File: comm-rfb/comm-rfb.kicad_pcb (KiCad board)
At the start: 4 copper layers, 90.2 x 95.9 mm, 5 parts, among them J1 PC104_Connector

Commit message: comm-rfb: reduce number of sheets in schematic
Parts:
- added C1: 12n, Capacitor_SMD:C_0402_1005Metric, F.Cu at (140.7, 115.6)
- added C10: 10p, Capacitor_SMD:C_0603_1608Metric, F.Cu at (168.4, 105.4)
- added C11: 0.1uF, Capacitor_SMD:C_0603_1608Metric, F.Cu at (192.3, 97.3)
- added C12: 10u, Capacitor_SMD:C_0603_1608Metric, F.Cu at (163.1, 112.4)
- added C13: 100n, Capacitor_SMD:C_0603_1608Metric, F.Cu at (172.4, 105.4)
- added C14: 100n, Capacitor_SMD:C_0603_1608Metric, F.Cu at (164.4, 105.4)
- added C15: 10n, Capacitor_SMD:C_0603_1608Metric, F.Cu at (167.2, 107.9)
- added C16: 1u, Capacitor_SMD:C_0603_1608Metric, F.Cu at (159.1, 112.4)
- added C17: 1u, Capacitor_SMD:C_0603_1608Metric, F.Cu at (171.2, 107.9)
- added C18: 100u, Capacitor_SMD:C_0603_1608Metric, F.Cu at (167.2, 112.9)
- added C19: 100n, Capacitor_SMD:C_0603_1608Metric, F.Cu at (177.1, 90.2)
- added C2: 20p, Capacitor_SMD:C_0402_1005Metric, F.Cu at (143.6, 111.6)
- added C20: 22u, Capacitor_SMD:C_0805_2012Metric, F.Cu at (164.8, 89.2)
- added C21: 22u, Capacitor_SMD:C_0805_2012Metric, F.Cu at (174.7, 87.5)
- added C3: 1000p, Capacitor_SMD:C_0402_1005Metric, F.Cu at (140.7, 113.6)
- added C4: 1000p, Capacitor_SMD:C_0402_1005Metric, F.Cu at (152.0, 105.1)
- added C5: 1000p, Capacitor_SMD:C_0402_1005Metric, F.Cu at (146.5, 109.6)
- added C6: 10p, Capacitor_SMD:C_0402_1005Metric, F.Cu at (143.6, 113.6)
- added C7: 10p, Capacitor_SMD:C_0402_1005Metric, F.Cu at (149.1, 107.1)
- added C8: 1p8, Capacitor_SMD:C_0402_1005Metric, F.Cu at (140.7, 111.6)
- added C9: 10p, Capacitor_SMD:C_0603_1608Metric, F.Cu at (167.2, 110.4)
- added D1: LED, LED_SMD:LED_0603_1608Metric, F.Cu at (183.0, 80.7)
- added D3: RED, Diode_SMD:D_0603_1608Metric, F.Cu at (188.4, 97.3)
- added FB1: 100R @ 100 MHz, Inductor_SMD:L_0603_1608Metric, F.Cu at (178.9, 87.2)
- added FB2: 100R @ 100MHz, Inductor_SMD:L_0603_1608Metric, F.Cu at (159.1, 109.9)
- added FB4: 100R @ 100 MHz, Daughterboard_footprints:BEADC1608X75N, F.Cu at (180.7, 101.9)
- added J10: Conn_02x04_Counter_Clockwise, Connector_PinSocket_2.54mm:PinSocket_2x04_P2.54mm_Vertical, F.Cu at (183.1, 121.7)
- added J11: Conn_02x06_Odd_Even, Connector_PinSocket_2.54mm:PinSocket_2x06_P2.54mm_Horizontal, F.Cu at (160.0, 121.7)
- added J12: Conn_02x05_Counter_Clockwise, Connector_PinSocket_2.54mm:PinSocket_2x05_P2.54mm_Horizontal, F.Cu at (175.9, 121.6)
- added J2: TFM-110-02-SM-D-A-K-TR, qset-footprints:SAMTEC_TFM-110-02-SM-D-A-K-TR, F.Cu at (130.5, 83.4)
- added J3: TFM-110-02-SM-D-A-K-TR, qset-footprints:SAMTEC_TFM-110-02-SM-D-A-K-TR, F.Cu at (149.0, 91.3)
- added J4: TFM-110-02-SM-D-A-K-TR, qset-footprints:SAMTEC_TFM-110-02-SM-D-A-K-TR, F.Cu at (130.5, 91.3)
- added J5: TFM-110-02-SM-D-A-K-TR, qset-footprints:SAMTEC_TFM-110-02-SM-D-A-K-TR, F.Cu at (149.0, 83.4)
- added J6: Conn_Coaxial, Connector_Coaxial:SMA_Amphenol_132134-10_Vertical, F.Cu at (125.5, 117.9)
- added J7: Conn_Coaxial, Connector_Coaxial:SMA_Amphenol_132134-10_Vertical, F.Cu at (134.7, 117.9)
- added J8: Conn_Coaxial, Connector_Coaxial:SMA_Amphenol_132134-10_Vertical, F.Cu at (134.7, 108.7)
- added J9: Conn_Coaxial, Connector_Coaxial:SMA_Amphenol_132134-10_Vertical, F.Cu at (125.5, 108.7)
- added L1: 150n, Inductor_SMD:L_0402_1005Metric, F.Cu at (149.1, 105.2)
- added L2: 22n, Inductor_SMD:L_0402_1005Metric, F.Cu at (143.6, 109.7)
- added MAX4372F1: MAX4372FESA+, STM32_Breakout:SOIC127P600X175-8N, F.Cu at (176.7, 82.7)
- added R1: 9.1k, Resistor_SMD:R_0603_1608Metric, F.Cu at (145.7, 105.4)
- added R10: 10k, Resistor_SMD:R_0603_1608Metric, F.Cu at (163.1, 109.9)
- added R2: 330, Resistor_SMD:R_0402_1005Metric, F.Cu at (140.7, 109.7)
- added R3: 15, Resistor_SMD:R_0402_1005Metric, F.Cu at (145.1, 107.7)
- added R4: 1k5, Resistor_SMD:R_0603_1608Metric, F.Cu at (183.0, 83.2)
- added R5: 100m, Resistor_SMD:R_0603_1608Metric, F.Cu at (173.1, 90.2)
- added R9: 2.2k, Resistor_SMD:R_0603_1608Metric, F.Cu at (184.7, 101.9)
- added TP1: TestPoint, TestPoint:TestPoint_Pad_D2.0mm, F.Cu at (169.1, 89.7)
- added U1: STM32F030CCT6, qset-footprints:QFP50P900X900X160-48N, F.Cu at (192.0, 73.9)
- added U2: SKY67150-396LF, qset-footprints:SON50P200X200X80-9N, F.Cu at (141.5, 105.9)
- added U3: AMS1117-3.3, Package_TO_SOT_SMD:SOT-223-3_TabPin2, F.Cu at (167.5, 83.5)
- added U4: MCP9808T-E/MC, qset-footprints:MCP9808T-E&slash_MC, F.Cu at (193.8, 111.8)
- added Y1: 16 MHz, Crystal:Crystal_SMD_3225-4Pin_3.2x2.5mm, F.Cu at (159.8, 106.4)
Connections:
- J1 pad 1: unconnected-(J1-Pad1) -> COMM-TXD
- J1 pad 2: unconnected-(J1-Pad2) -> COMM-RXD
- J1 pad 3: unconnected-(J1-Pad3) -> COMM-CTS
- J1 pad 32: unconnected-(J1-Pad32) -> 5V0-CHG
- J1 pad 4: unconnected-(J1-Pad4) -> COMM-RTS
- J1 pad 61: unconnected-(J1-Pad61) -> GND
- J1 pad 66: unconnected-(J1-Pad66) -> GND
- J1 pad 67: unconnected-(J1-Pad67) -> SW6-5V
- J1 pad 69: unconnected-(J1-Pad69) -> GND
- J1 pad 72: unconnected-(J1-Pad72) -> GND
- J1 pad 73: unconnected-(J1-Pad73) -> GND
- J1 pad 74: unconnected-(J1-Pad74) -> GND
- J1 pad 81: unconnected-(J1-Pad81) -> GND
- J1 pad 82: unconnected-(J1-Pad82) -> GND
- J1 pad 84: unconnected-(J1-Pad84) -> GND

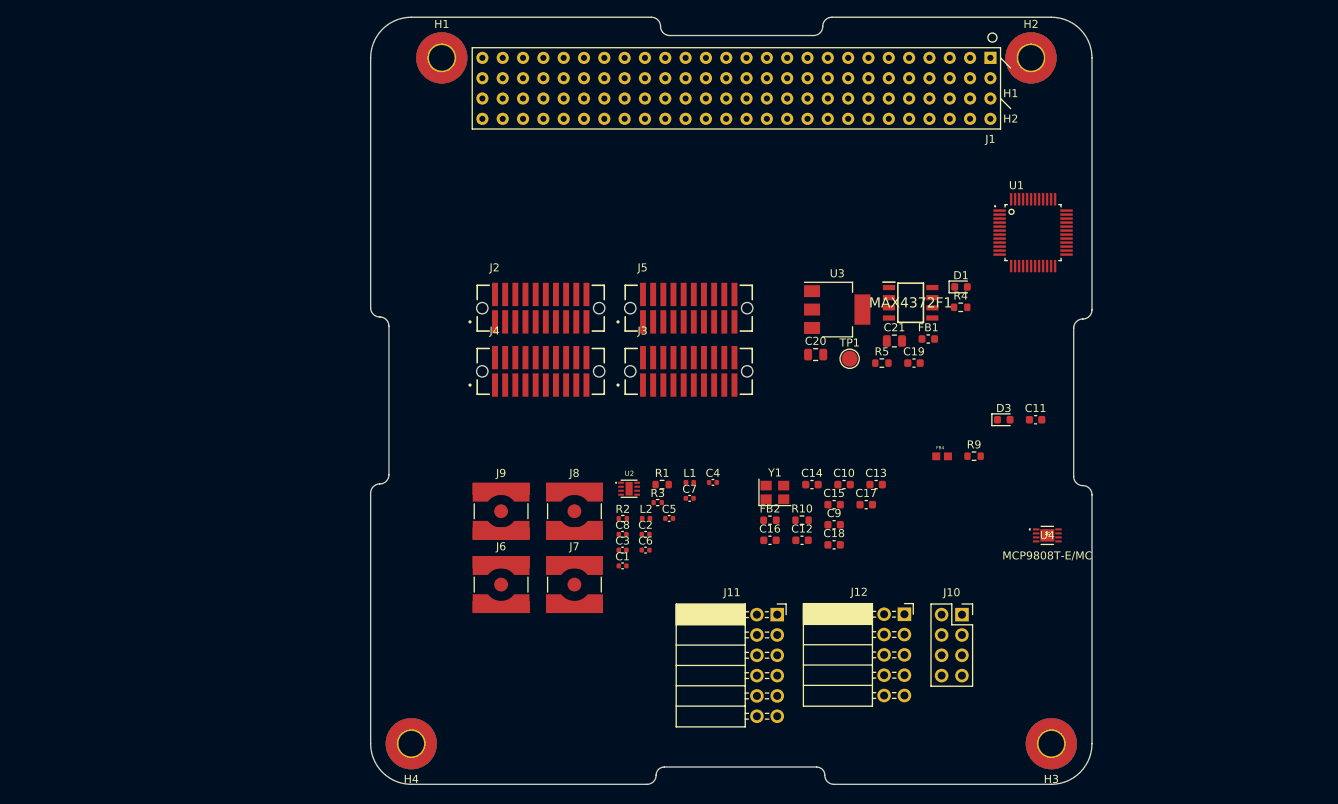
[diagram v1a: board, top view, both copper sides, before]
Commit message: possible layout -no connections
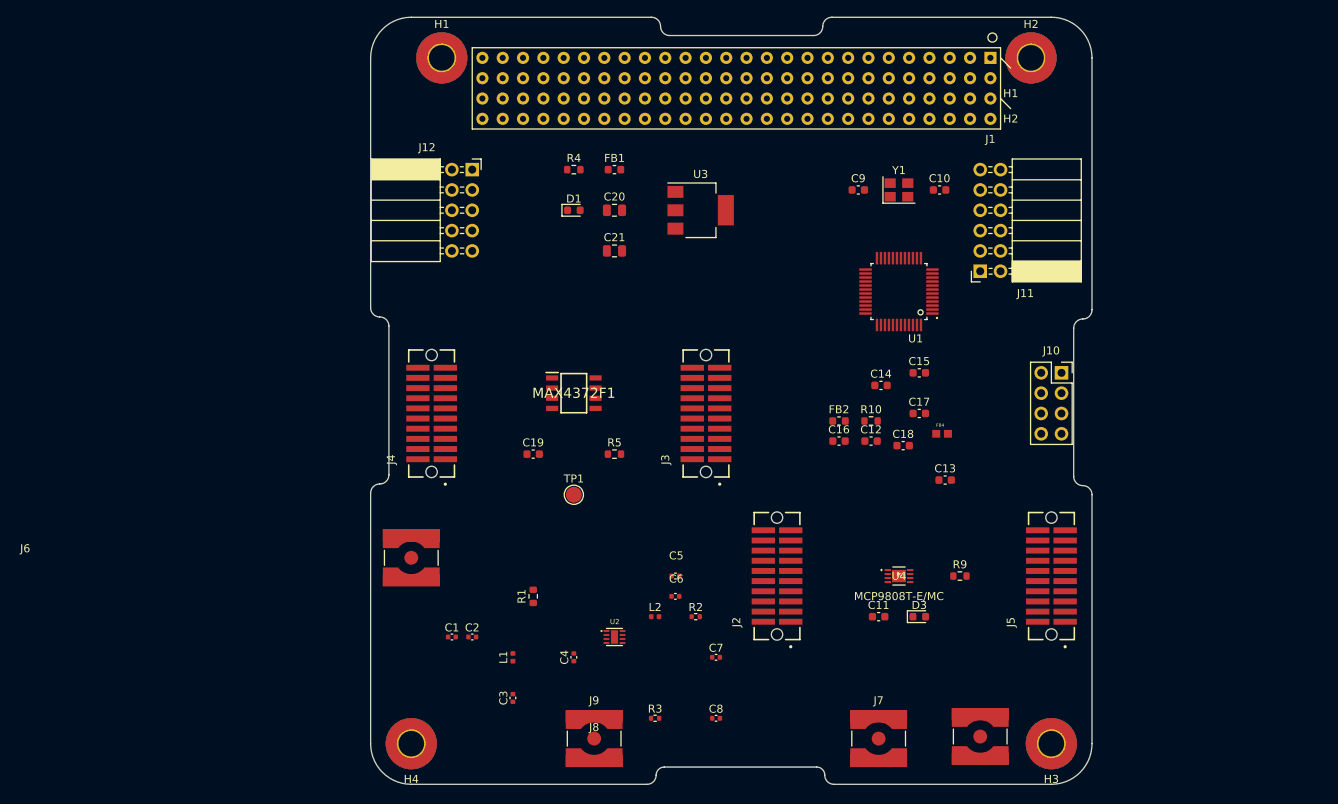
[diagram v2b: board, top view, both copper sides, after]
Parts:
- moved J12 77.5 mm to (121.9, 66.0)
- moved J8 58.0 mm to (185.4, 136.9)
- moved J5 56.4 mm to (194.3, 116.8), turned to 90 degrees
- moved R4 51.3 mm to (134.6, 66.0)
- moved J11 49.9 mm to (185.4, 78.7), turned to 180 degrees
- moved D1 49.3 mm to (134.6, 71.1)
- moved C19 48.9 mm to (129.5, 101.6)
- moved J2 44.7 mm to (160.0, 116.8), turned to 90 degrees
- moved FB1 44.6 mm to (139.7, 66.0)
- moved MAX4372F1 43.6 mm to (134.6, 94.0)
- moved J7 42.6 mm to (172.7, 137.2)
- moved C9 42.0 mm to (170.2, 68.6)
- moved Y1 40.9 mm to (175.3, 68.6)
- moved C10 38.7 mm to (180.3, 68.6)
- moved TP1 38.4 mm to (134.6, 106.7)
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
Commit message: initial routing done ~ fix bug still
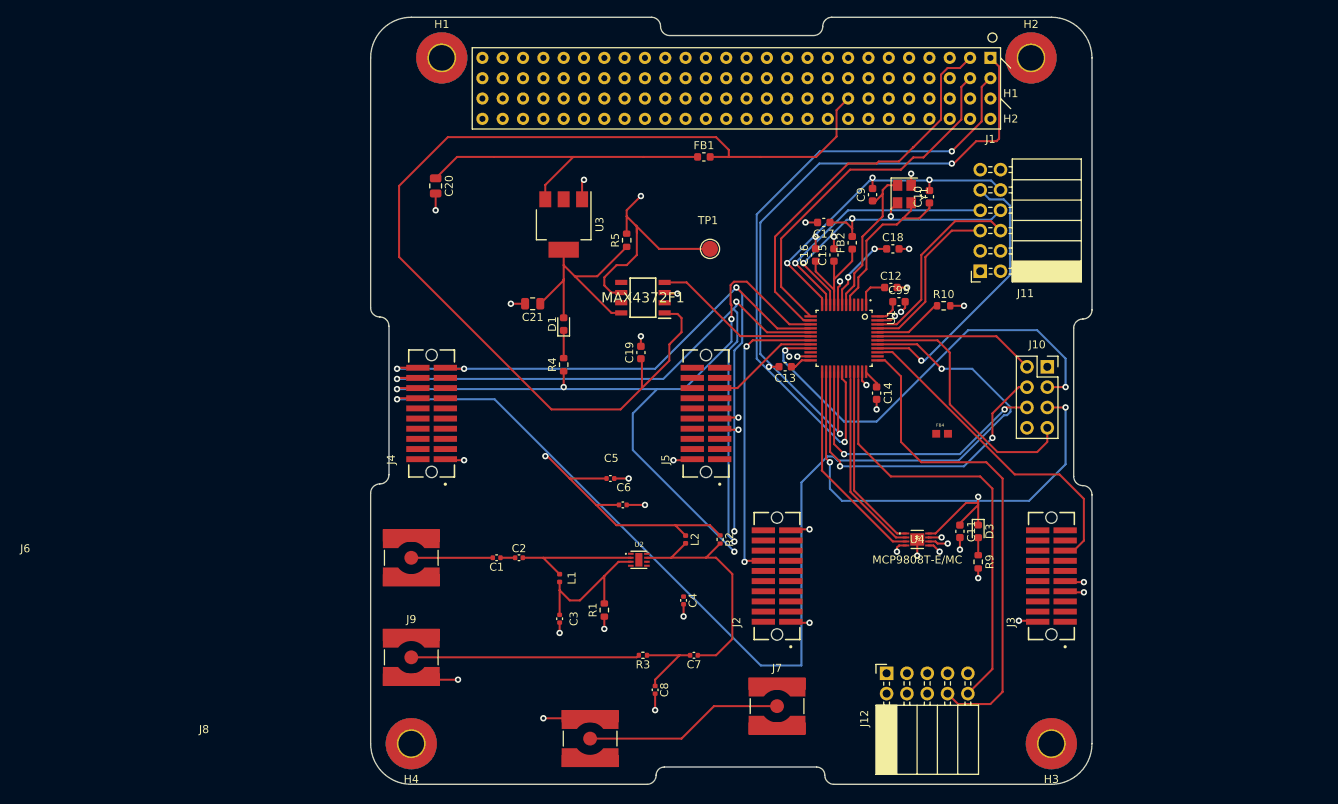
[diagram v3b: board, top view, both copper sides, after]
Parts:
- added C99: 100n, Capacitor_SMD:C_0603_1608Metric, F.Cu at (175.3, 82.5)
- C12: value 10u -> 100n
- moved J12 81.5 mm to (173.7, 129.0), turned to 90 degrees
- moved J8 48.8 mm to (136.7, 137.2)
- moved J3 47.7 mm to (194.3, 116.8)
- moved J5 47.7 mm to (151.1, 96.5)
- moved TP1 35.1 mm to (151.6, 75.9)
- moved R5 26.8 mm to (141.2, 74.9), turned to 90 degrees
- moved C17 26.7 mm to (165.9, 72.6), turned to 180 degrees
- moved J9 25.0 mm to (114.3, 127.0)
- moved C18 24.6 mm to (174.5, 75.9)
- moved C13 24.5 mm to (161.0, 90.7), turned to 180 degrees
- moved R4 24.4 mm to (133.3, 90.4), turned to 90 degrees
- moved C16 23.4 mm to (164.8, 76.7), turned to 90 degrees
- moved C20 22.6 mm to (117.3, 68.1), turned to -90 degrees
- moved FB2 22.3 mm to (169.4, 75.2), turned to 90 degrees
- moved C12 19.4 mm to (174.2, 80.8)
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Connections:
- U1 pad 10: sys-GPIO1 -> SYS-GPIO1
- U1 pad 11: sys-GPIO2 -> SYS-GPIO2
- U1 pad 12: sys-GPIO3 -> SYS-GPIO3
- U1 pad 40: sys-GPIO4 -> SYS-GPIO4
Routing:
- net SPI1-CSN-TX: track 0.00 -> 140.5 mm, vias 0 -> 2
- net SW6-5V: track 0.00 -> 132.6 mm
- net +3V3: track 0.00 -> 109.8 mm, vias 0 -> 9
- net SPI1-SCLK: track 0.00 -> 93.3 mm, vias 0 -> 3
- net SPI1-MISO: track 0.00 -> 91.8 mm, vias 0 -> 3
- net SPI1-MOSI: track 0.00 -> 90.4 mm, vias 0 -> 3
- net GND: track 0.00 -> 86.8 mm, vias 0 -> 43
- net COMM-TXD: track 0.00 -> 83.1 mm, vias 0 -> 2
- net COMM-RXD: track 0.00 -> 81.4 mm, vias 0 -> 2
- net SWCLK: track 0.00 -> 61.3 mm
- net SPI2-IRQ: track 0.00 -> 56.2 mm, vias 0 -> 2
- net SPI2-SCLK: track 0.00 -> 55.2 mm, vias 0 -> 2
- net SWDIO: track 0.00 -> 54.1 mm
- net COMM-CTS: track 0.00 -> 49.7 mm
- net COMM-RTS: track 0.00 -> 45.6 mm
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- added copper zone on In2.Cu, net +3V3
- added copper zone on In1.Cu, net GND

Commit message: made PA smaller, added some missing GND connections, and connect AMP-ENABLE
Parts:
- moved R2 17.0 mm to (135.9, 112.5)
- moved C7 15.3 mm to (138.4, 116.3), turned to -90 degrees
- moved C4 15.0 mm to (133.3, 118.9)
- moved L2 14.5 mm to (134.1, 112.5)
- moved R3 12.1 mm to (131.6, 123.7)
- moved U2 11.7 mm to (131.1, 114.8)
- moved C8 11.5 mm to (136.7, 123.0)
- moved R1 10.1 mm to (128.5, 119.1)
- moved C3 8.19 mm to (125.5, 118.6)
- moved L1 7.43 mm to (125.5, 116.1)
- moved C6 7.30 mm to (133.6, 109.5)
- moved C5 7.06 mm to (133.1, 108.2)
- moved C1 5.11 mm to (119.9, 114.6)
- moved C2 5.11 mm to (122.7, 114.6)
- moved C13 1.61 mm to (161.5, 92.2)
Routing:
- net AMP-ENABLE: track 0.01 -> 55.2 mm, vias 1 -> 2
- net +3V3: track 109.8 -> 86.4 mm
- net Net-(C7-Pad1): track 29.8 -> 10.8 mm
- net /RF Front End (Tx & Rx)/AMP-TO-EXT: track 28.6 -> 18.1 mm
- net Net-(C3-Pad1): track 19.0 -> 9.85 mm
- net GND: track 86.8 -> 95.9 mm, vias 43 -> 45
- net Net-(C2-Pad2): track 16.4 -> 8.49 mm
- net /RF Front End (Tx & Rx)/EM-TO-AMP: track 10.2 -> 5.08 mm
- net Net-(C7-Pad2): track 10.5 -> 14.9 mm

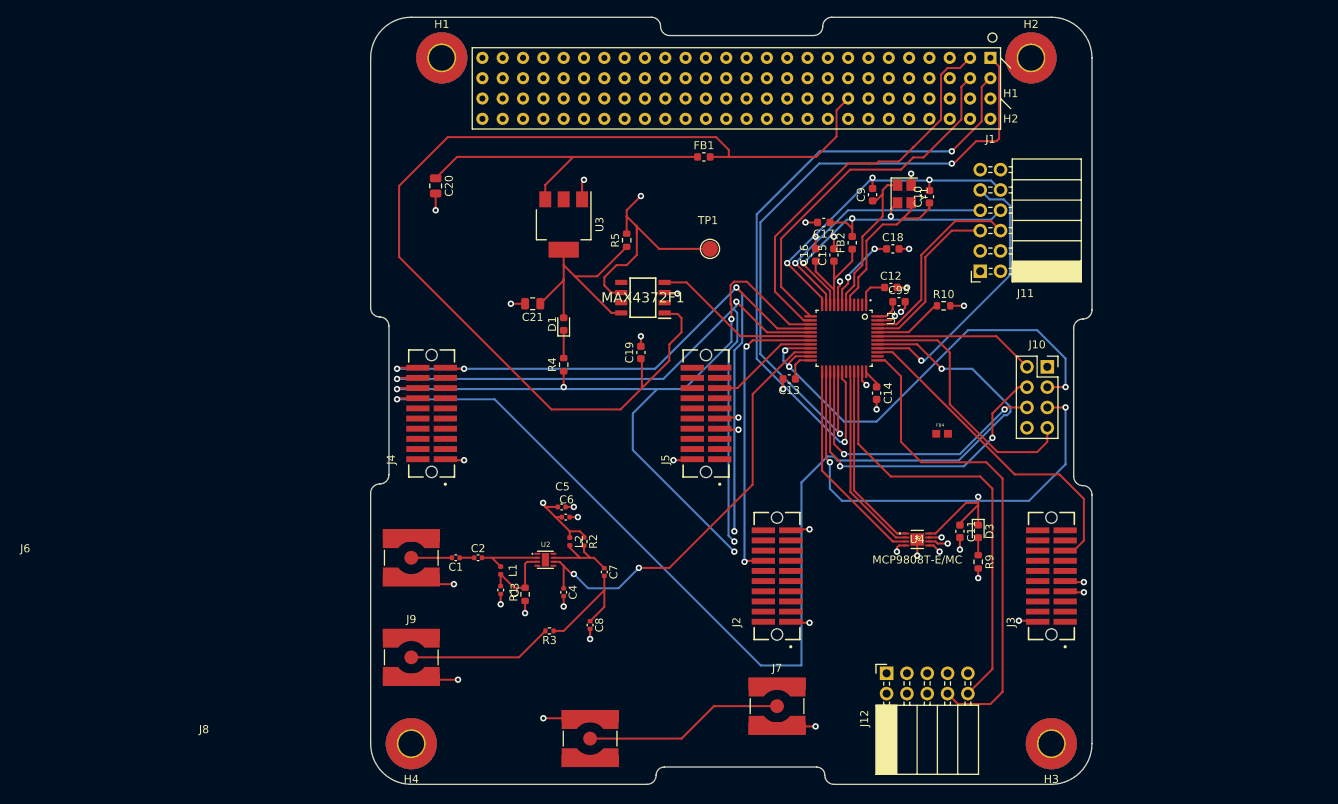
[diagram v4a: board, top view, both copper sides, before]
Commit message: comm-rfb: include correct spacing for cc1120-em connectors, remove traces
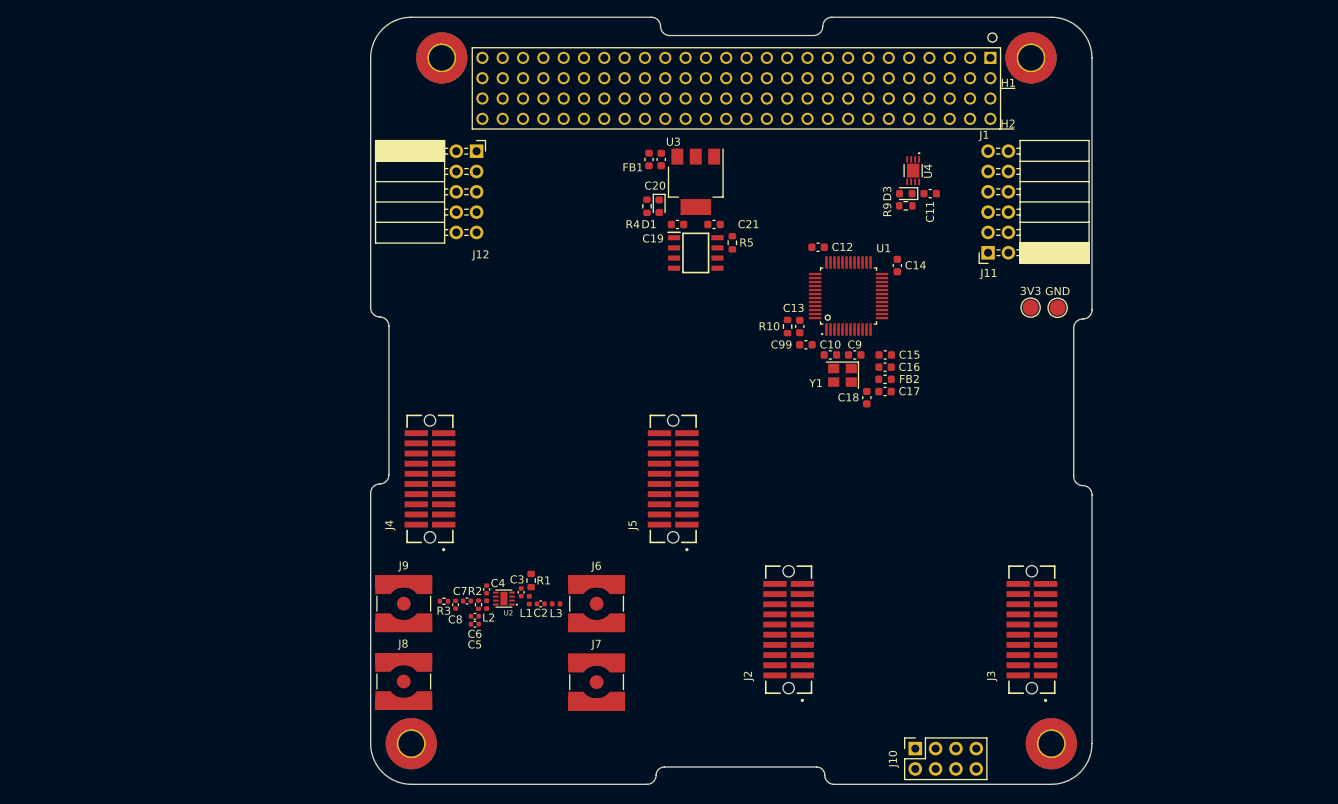
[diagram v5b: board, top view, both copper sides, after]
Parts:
- removed C1: 12n, Capacitor_SMD:C_0402_1005Metric
- removed FB4: 100R @ 100 MHz, Daughterboard_footprints:BEADC1608X75N
- added L3: 12n, Inductor_SMD:L_0402_1005Metric, F.Cu at (132.4, 120.3)
- added TP2: GND, TestPoint:TestPoint_Pad_D2.0mm, F.Cu at (195.1, 83.3)
- C20, C21: footprint Capacitor_SMD:C_0805_2012Metric -> Capacitor_SMD:C_0603_1608Metric
- J1: footprint pc104-connector:pc104-connector -> pc104-template:pc104-connector
- J10: value Conn_02x04_Counter_Clockwise -> Radio Test Connector
- J11: value Conn_02x06_Odd_Even -> System Test Connector
- J12: value Conn_02x05_Counter_Clockwise -> Programming Header
- TP1: value TestPoint -> 3V3
- moved J12 83.0 mm to (122.5, 63.7), turned to 0 degrees
- moved J10 50.5 mm to (177.3, 138.4), turned to 90 degrees
- moved U4 46.1 mm to (177.0, 66.2), turned to -90 degrees
- moved R9 45.4 mm to (176.1, 70.6), turned to 0 degrees
- moved D3 43.2 mm to (176.1, 69.0), turned to 180 degrees
- moved C11 42.4 mm to (179.2, 69.0), turned to 0 degrees
- moved TP1 40.7 mm to (191.7, 83.3), turned to 180 degrees
- moved C20 28.4 mm to (145.5, 64.8)
- moved C21 24.7 mm to (152.1, 72.9), turned to 0 degrees
- moved J8 24.4 mm to (113.4, 130.0)
- moved Y1 23.9 mm to (168.2, 91.7), turned to 180 degrees
- moved J6 23.9 mm to (137.5, 120.3)
- moved C10 23.3 mm to (166.7, 89.2), turned to 180 degrees
- moved J7 22.8 mm to (137.5, 130.1)
- moved C17 22.5 mm to (173.5, 93.8)
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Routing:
- net SPI1-CSN-TX: track 140.5 -> 0.00 mm, vias 2 -> 0
- net SW6-5V: track 132.6 -> 0.00 mm
- net GND: track 95.9 -> 0.36 mm, vias 45 -> 0
- net SPI1-SCLK: track 93.3 -> 0.00 mm, vias 3 -> 0
- net SPI1-MISO: track 91.8 -> 0.00 mm, vias 3 -> 0
- net SPI1-MOSI: track 90.4 -> 0.00 mm, vias 3 -> 0
- net +3V3: track 86.4 -> 0.00 mm, vias 9 -> 0
- net COMM-TXD: track 83.1 -> 0.00 mm, vias 2 -> 0
- net COMM-RXD: track 81.4 -> 0.00 mm, vias 2 -> 0
- net SWCLK: track 61.3 -> 0.00 mm
- net SPI2-IRQ: track 56.2 -> 0.00 mm, vias 2 -> 0
- net AMP-ENABLE: track 55.2 -> 0.00 mm, vias 2 -> 0
- net SPI2-SCLK: track 55.2 -> 0.00 mm, vias 2 -> 0
- net SWDIO: track 54.1 -> 0.00 mm
- net COMM-CTS: track 49.7 -> 0.00 mm
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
